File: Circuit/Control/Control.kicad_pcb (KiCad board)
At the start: 2 copper layers, 55.9 x 22.9 mm, 34 parts, among them J1 Signal, J2 12V NO G, Q1 2N2222, SW1 Force on, U1 LM393, U2 NE555

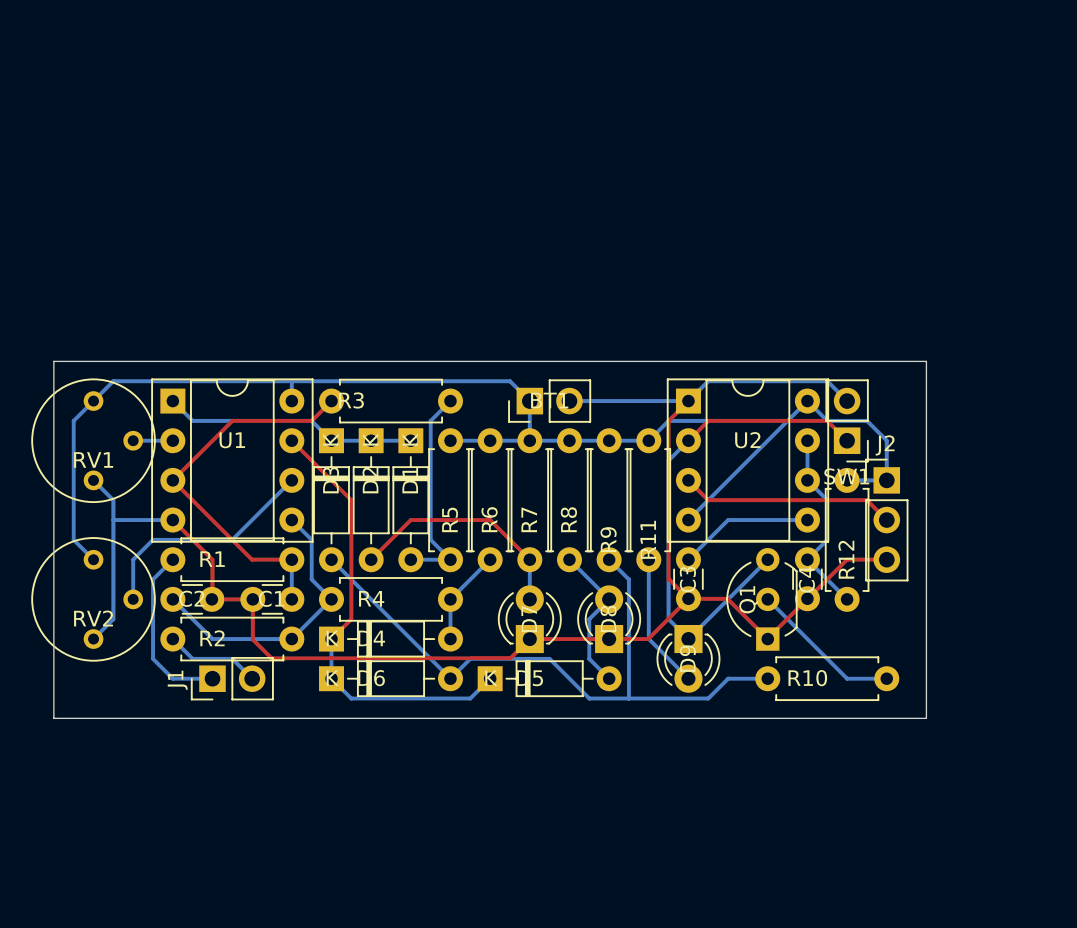
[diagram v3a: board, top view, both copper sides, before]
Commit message: [Circuit] One channel voltage sensing and control modules
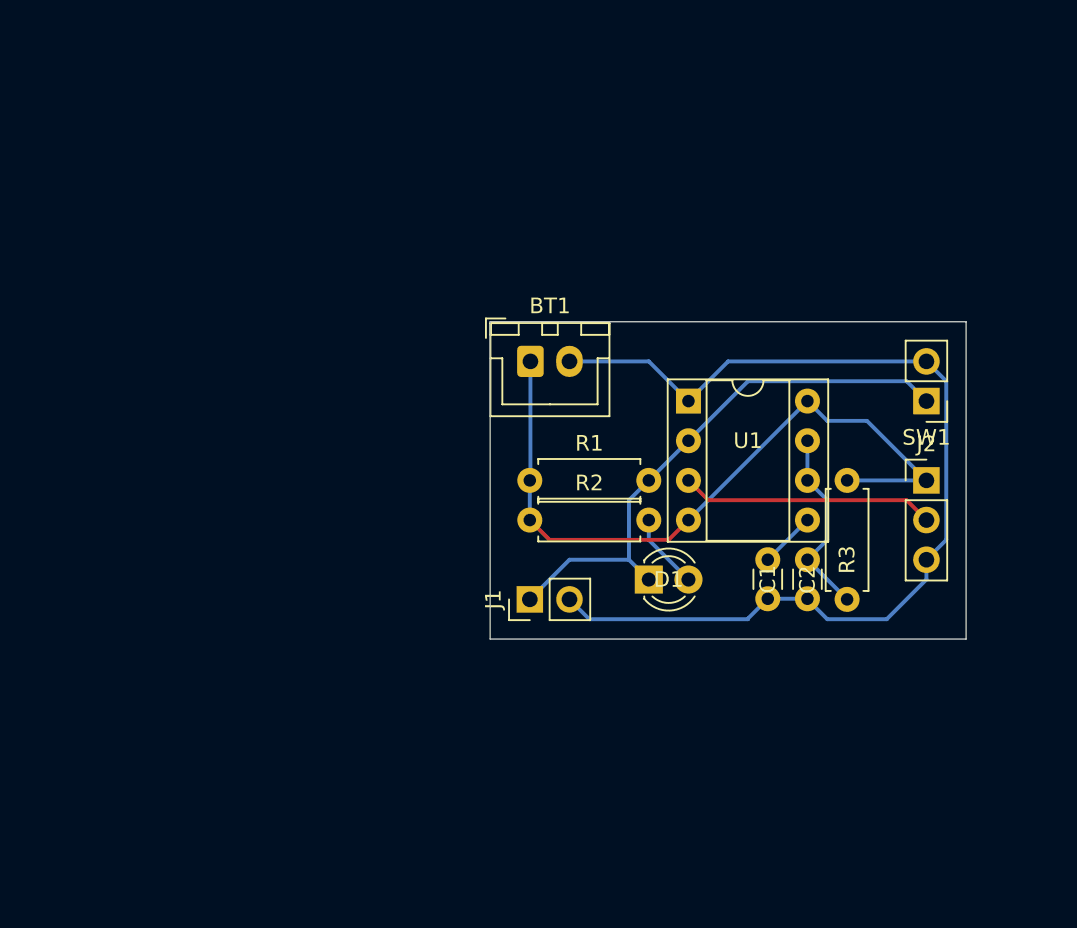
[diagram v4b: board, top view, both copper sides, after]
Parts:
- removed the C1 at (134.6, 81.3)
- removed the C2 at (127.0, 81.3)
- removed the D1 at (142.2, 71.1)
- removed D2, D3, D4, D5, D6: 1N4148, Diode_THT:D_DO-35_SOD27_P7.62mm_Horizontal
- removed D7, D8: LED, LED_THT:LED_D3.0mm_FlatTop
- removed Q1: 2N2222, Package_TO_SOT_THT:TO-92_Inline_Wide
- removed R10, R9: 3K3, Resistor_THT:R_Axial_DIN0207_L6.3mm_D2.5mm_P7.62mm_Horizontal
- removed R11, R5, R6, R7, R8: 2K, Resistor_THT:R_Axial_DIN0207_L6.3mm_D2.5mm_P7.62mm_Horizontal
- removed the R3 at (137.2, 68.6)
- removed R4: 220K, Resistor_THT:R_Axial_DIN0207_L6.3mm_D2.5mm_P7.62mm_Horizontal
- removed RV1, RV2: 50K, Potentiometer_THT:Potentiometer_Bourns_3339P_Vertical
- removed the U1 at (127.0, 68.6)
- BT1: footprint Connector_PinHeader_2.54mm:PinHeader_1x02_P2.54mm_Vertical -> Connector_JST:JST_XH_B2B-XH-A_1x02_P2.50mm_Vertical
- R1: value 1K -> 3K3
- R2: value 1K -> 2K
- moved J1 20.9 mm to (149.9, 81.3)
- moved R2 17.0 mm to (149.9, 76.2), turned to 0 degrees
- moved R1 16.1 mm to (149.9, 73.7), turned to 0 degrees
- moved SW1 5.68 mm to (175.3, 68.6)
- moved C1 5.08 mm to (165.1, 78.7)
- moved D1 4.58 mm to (157.5, 80.0), turned to 0 degrees
- moved BT1 2.54 mm to (149.9, 66.0), turned to 0 degrees
- moved J2 2.54 mm to (175.3, 73.7)
- renumbered C3 to C1, C4 to C2, D9 to D1, R12 to R3, U2 to U1
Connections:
- D1 pad 1: Net-(D9-Pad1) -> Net-(D1-Pad1)
- D1 pad 2: Net-(D9-Pad2) -> Net-(D1-Pad2)
- J1 pad 1: /CapacitorSignal1 -> Net-(D1-Pad1)
- J1 pad 2: /CapacitorSignal2 -> GND
- R1 pad 1: Net-(C1-Pad1) (its old number) -> +12V
- R1 pad 2: /CapacitorSignal1 -> Net-(D1-Pad1)
- R2 pad 1: Net-(C2-Pad1) (its old number) -> +12V
- R2 pad 2: /CapacitorSignal2 -> Net-(D1-Pad2)
- SW1 pad 1: Net-(D9-Pad1) -> Net-(D1-Pad1)
- U1 pad 2: Net-(D9-Pad1) -> Net-(D1-Pad1)
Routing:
- net Net-(D3-Pad2): track 42.6 -> 0.00 mm
- net +12V: track 88.2 -> 47.0 mm
- net GND: track 104.9 -> 65.6 mm
- net Net-(D9-Pad1): track 32.1 -> 0.00 mm
- net Net-(D4-Pad1): track 28.6 -> 0.00 mm
- net Net-(C1-Pad1) (its old number): track 24.5 -> 0.00 mm
- net Net-(D1-Pad1): track 16.3 -> 35.7 mm
- net Net-(C2-Pad1) (its old number): track 18.5 -> 0.00 mm
- net Net-(RV2-Pad2): track 14.8 -> 0.00 mm
- net Net-(D2-Pad2): track 14.8 -> 0.00 mm
- net /CapacitorSignal1: track 11.2 -> 0.00 mm
- net Net-(D5-Pad2): track 9.72 -> 0.00 mm
- net Net-(Q1-Pad2): track 9.72 -> 0.00 mm
- net Net-(D1-Pad2): track 13.8 -> 4.86 mm
- net Net-(D9-Pad2): track 8.67 -> 0.00 mm
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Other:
- board size 55.9 x 22.9 mm -> 30.5 x 20.3 mm
- board text removed: "M. Gong"

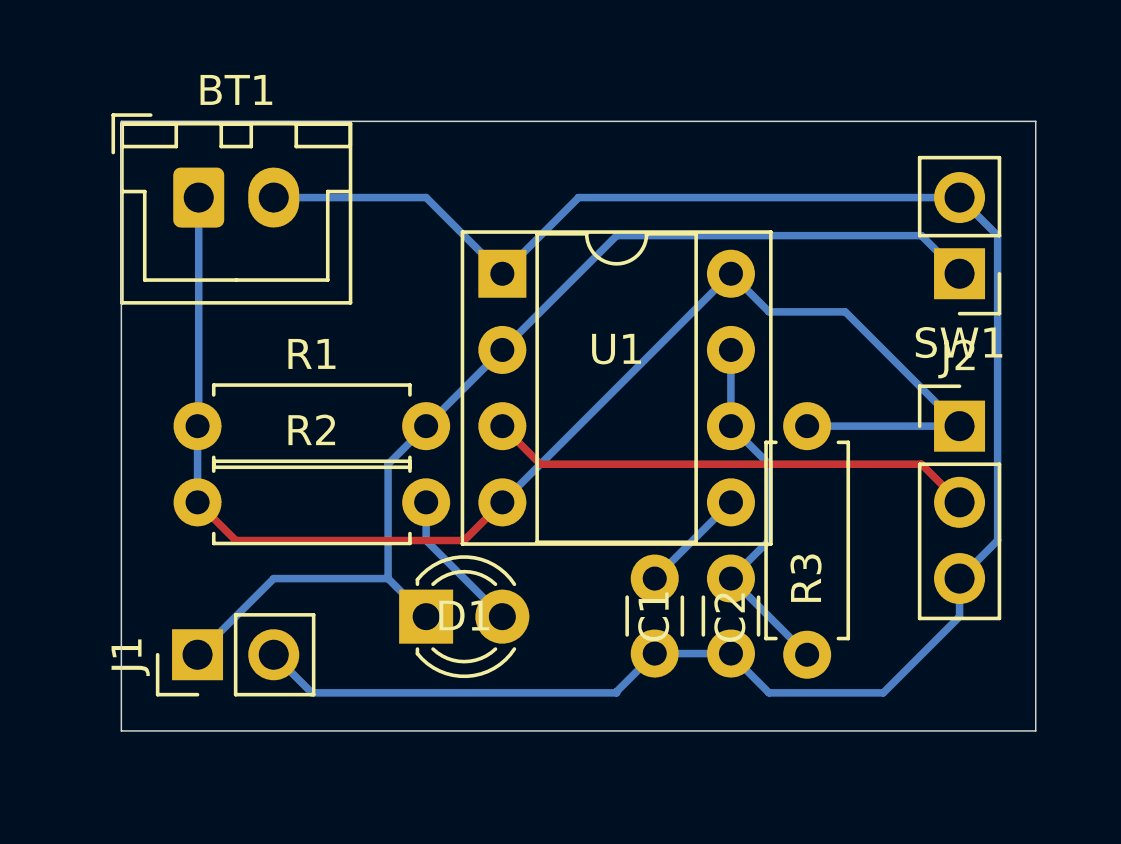
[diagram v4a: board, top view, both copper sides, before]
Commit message: [Circuit] Adjustable delay in control module
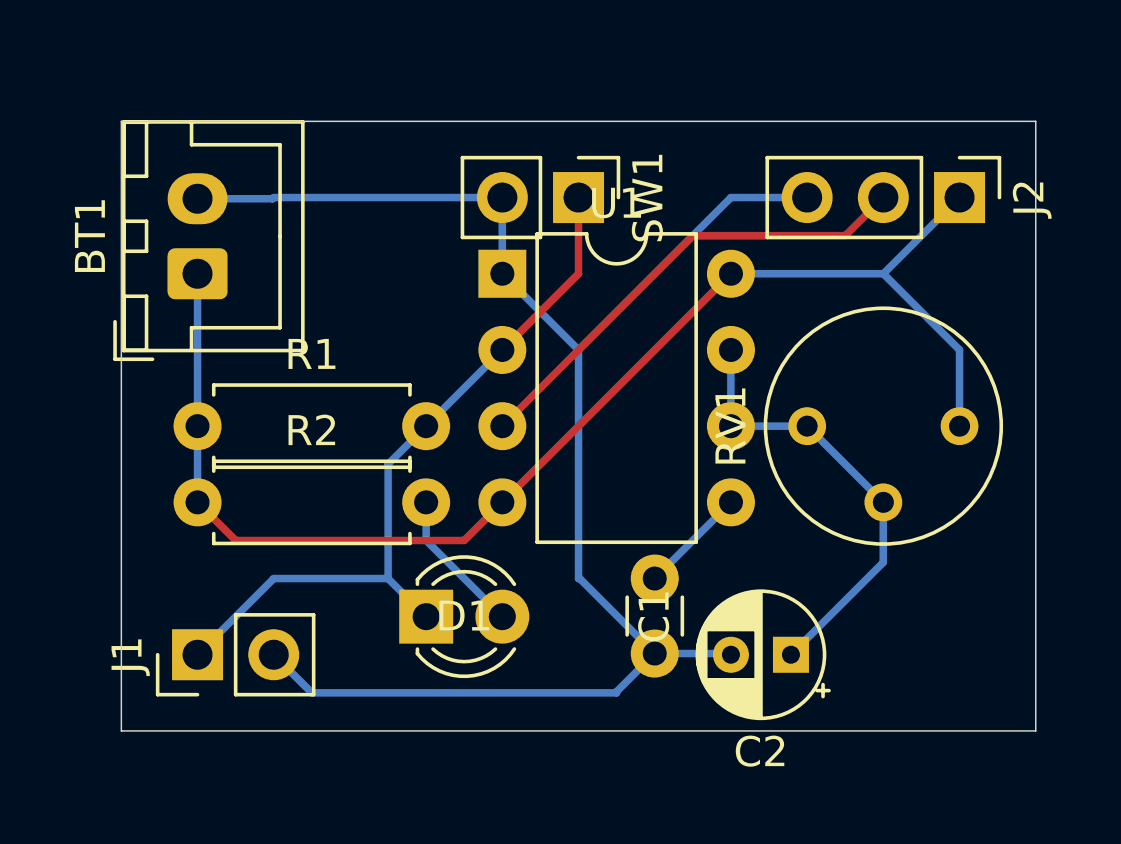
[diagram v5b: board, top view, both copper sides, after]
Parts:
- removed R3: 220K, Resistor_THT:R_Axial_DIN0207_L6.3mm_D2.5mm_P7.62mm_Horizontal
- added RV1: 50K, Potentiometer_THT:Potentiometer_Bourns_3339P_Vertical, F.Cu at (175.3, 73.7)
- C2: value 0.1uF -> 1uF; footprint Capacitor_THT:C_Disc_D3.0mm_W1.6mm_P2.50mm -> Capacitor_THT:CP_Radial_D4.0mm_P2.00mm
- U1: footprint Package_DIP:DIP-8_W7.62mm_Socket -> Package_DIP:DIP-8_W7.62mm
- moved SW1 13.0 mm to (162.6, 66.0), turned to 270 degrees
- moved J2 7.62 mm to (175.3, 66.0), turned to 270 degrees
- moved C2 3.23 mm to (169.6, 81.3), turned to 180 degrees
- moved BT1 2.54 mm to (149.9, 68.6), turned to 90 degrees
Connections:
- net Net-(D1-Pad1) renamed /CapacitorSignal
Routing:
- net GND: track 65.6 -> 53.6 mm
- net /CapacitorSignal: track 35.7 -> 24.5 mm
- net Net-(C2-Pad1): track 12.3 -> 15.0 mm
- net +12V: track 47.0 -> 44.5 mm

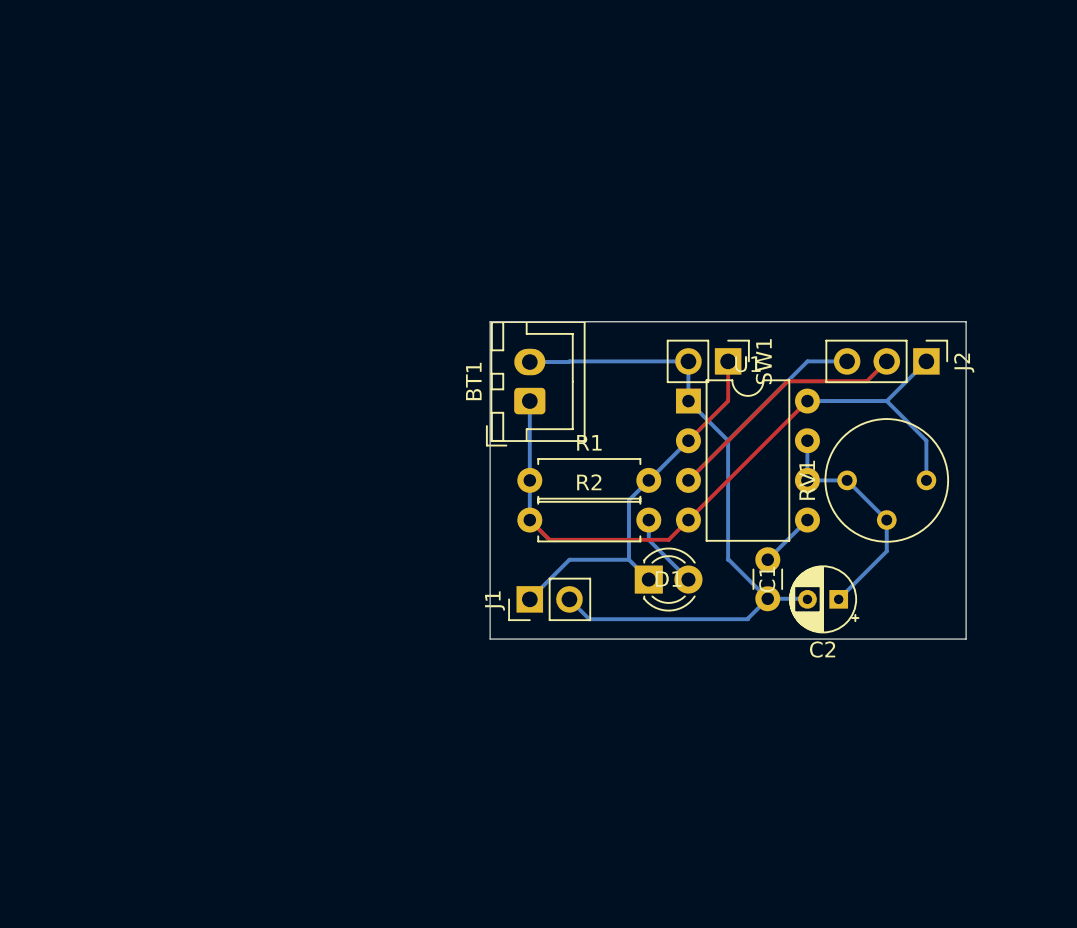
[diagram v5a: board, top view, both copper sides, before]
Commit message: [Circuit] Refine the control module
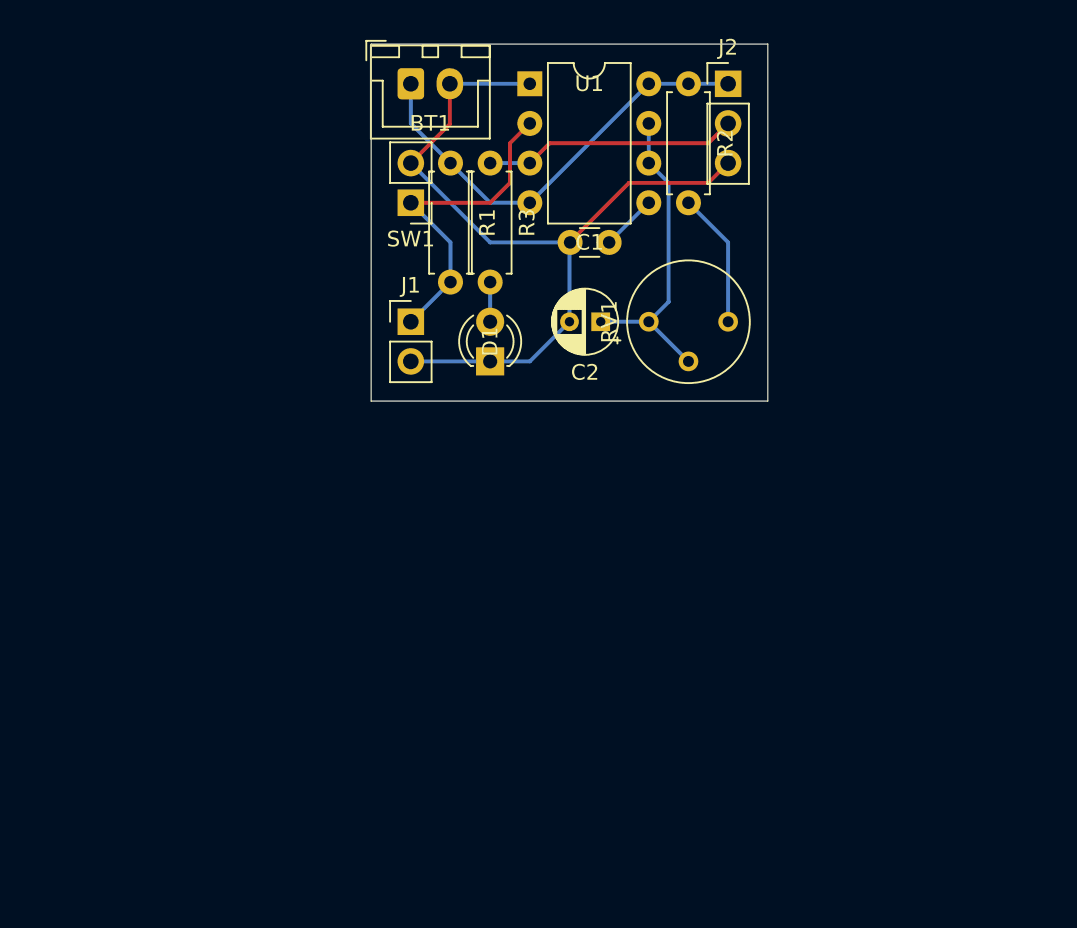
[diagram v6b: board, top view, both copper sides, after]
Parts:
- added R2: 2K, Resistor_THT:R_Axial_DIN0207_L6.3mm_D2.5mm_P7.62mm_Horizontal, F.Cu at (160.0, 48.3)
- R1: value 3K3 -> 3.3K
- moved C2 23.4 mm to (154.4, 63.5)
- moved R3 23.0 mm to (147.3, 53.3), turned to 270 degrees
- moved SW1 22.7 mm to (142.2, 55.9), turned to 180 degrees
- moved U1 22.7 mm to (149.9, 48.3)
- moved C1 22.7 mm to (154.9, 58.4), turned to 180 degrees
- moved J2 21.8 mm to (162.6, 48.3), turned to 0 degrees
- moved BT1 21.7 mm to (142.2, 48.3), turned to 0 degrees
- moved R1 20.9 mm to (144.8, 53.3), turned to 270 degrees
- moved J1 19.3 mm to (142.2, 63.5), turned to 0 degrees
- moved D1 17.3 mm to (147.3, 66.0), turned to 90 degrees
- moved RV1 16.3 mm to (162.6, 63.5)
- renumbered R2 to R3
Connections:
- D1 pad 1: /CapacitorSignal -> GND
- R3 pad 1: +12V -> /ControlSignal
- RV1 pad 1: +12V -> Net-(R2-Pad2)
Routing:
- net +12V: track 44.5 -> 28.1 mm
- net Net-(R2-Pad2): track 0.00 -> 8.67 mm
- net Net-(C2-Pad1): track 15.0 -> 20.4 mm
- net /CapacitorSignal: track 24.5 -> 20.9 mm
- net Net-(D1-Pad2): track 4.86 -> 2.54 mm
- net GND: track 53.6 -> 52.0 mm
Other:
- board size 30.5 x 20.3 mm -> 25.4 x 22.9 mm
